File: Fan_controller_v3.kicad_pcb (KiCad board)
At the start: 4 copper layers, 50 x 25 mm, 52 parts, among them J1 Load2, J2 Dig_mod_iface, K1 HFD2_005-S-L2-D_Split, K2 HFD2_005-S-L2-D_Split, Q1 2N5551S, Q2 2N5551S, Q3 BSS138, Q4 BSS138, Q5 2N5551S, Q6 2N5551S, U1 ADuM1251ARZ, U2 PCA9536DP

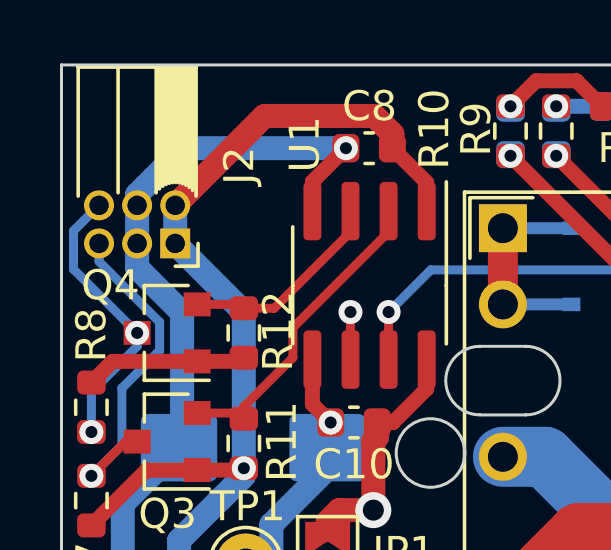
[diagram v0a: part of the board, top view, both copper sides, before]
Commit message: Сформирован перечень элементов, 3D-модель, исправлены ошибки, реализована панелизация платы.
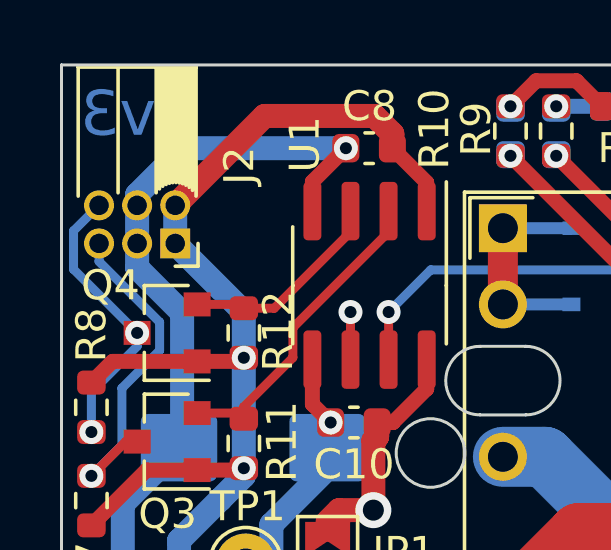
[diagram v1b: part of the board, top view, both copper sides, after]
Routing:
- net +5P: vias 1 -> 2
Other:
- board text added: "v3"

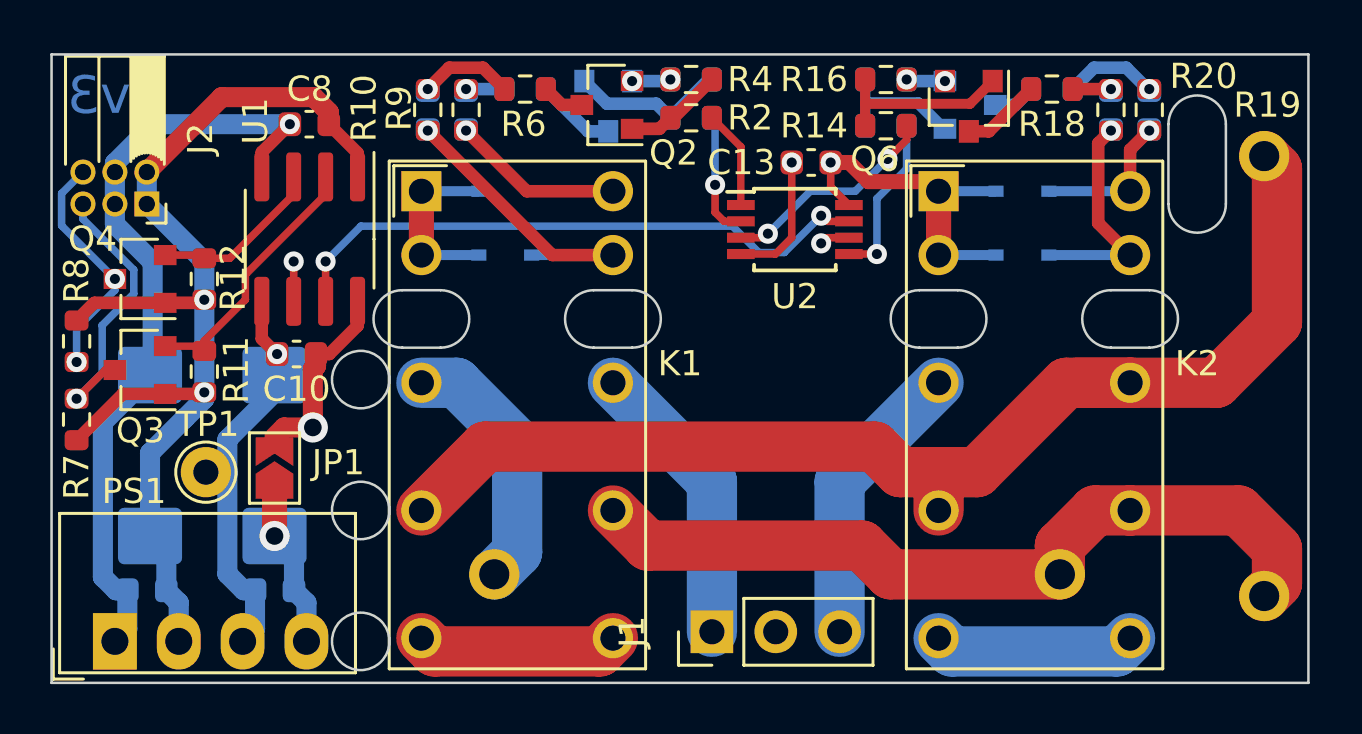
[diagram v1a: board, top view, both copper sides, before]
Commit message: Добавил отверстия в виде футпринтов и обновил гербера. Схему пока не менял.
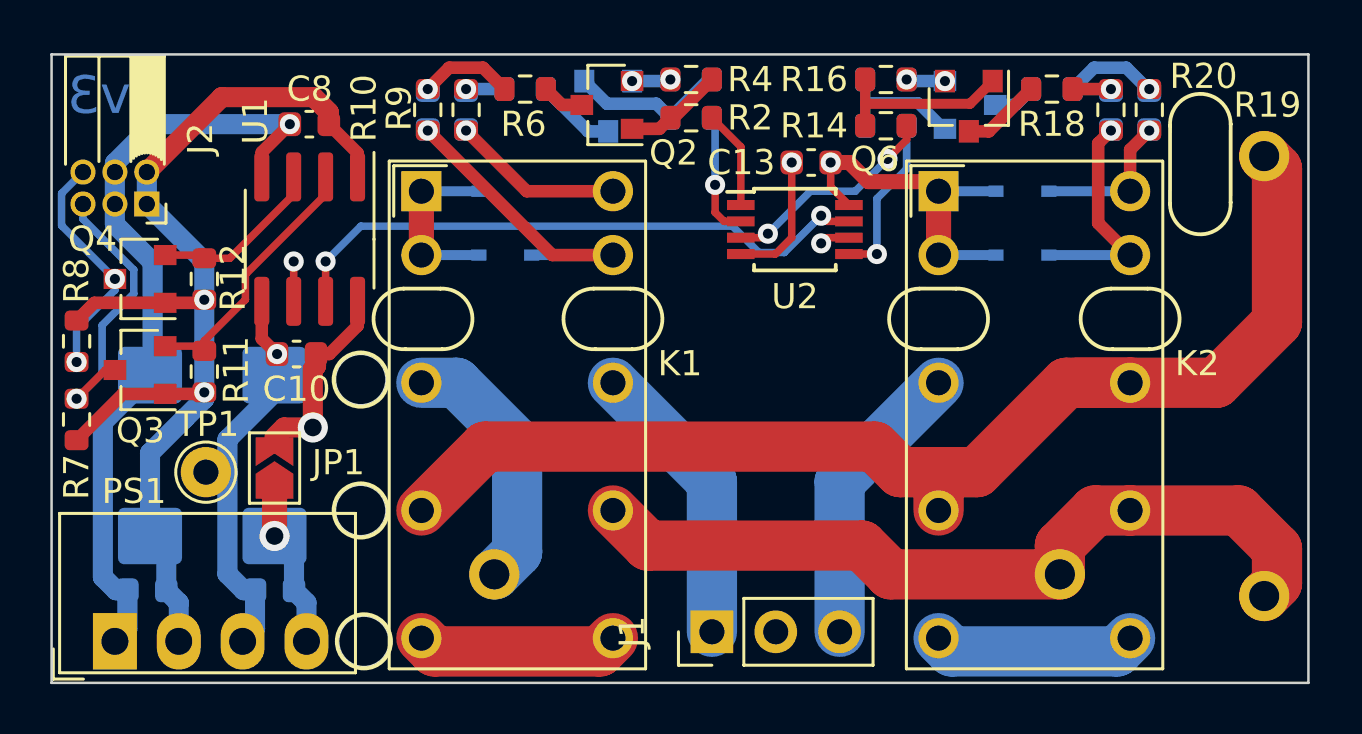
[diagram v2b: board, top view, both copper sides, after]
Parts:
- added REF**: MountingHole_2.29x5.46mm, Modules:MountingHole_2.29x5.46mm, F.Cu at (120.7, 79.4)
- added REF**: MountingHole_2.29x3.81mm, Modules:MountingHole_2.29x3.81mm, F.Cu at (117.9, 85.5)
- added REF**: MountingHole_2.29x3.81mm, Modules:MountingHole_2.29x3.81mm, F.Cu at (110.3, 85.5)
- added REF**: MountingHole_2.29x3.81mm, Modules:MountingHole_2.29x3.81mm, F.Cu at (97.3, 85.5)
- added REF**: MountingHole_2.29x3.81mm, Modules:MountingHole_2.29x3.81mm, F.Cu at (89.8, 85.5)
- added REF**: MountingHole_D2.0mm, Modules:MountingHole_D2.0mm, F.Cu at (87.3, 87.9)
- added REF**: MountingHole_D2.0mm, Modules:MountingHole_D2.0mm, F.Cu at (87.3, 93.1)
- added REF**: MountingHole_D2.0mm, Modules:MountingHole_D2.0mm, F.Cu at (87.4, 98.3)
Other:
- outline, holes or cut-outs redrawn

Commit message: Добавил изолирующие отверстия на схему. Подправил компоненты отверстий. Удалил контуры отверстий на обеих слоях платы.
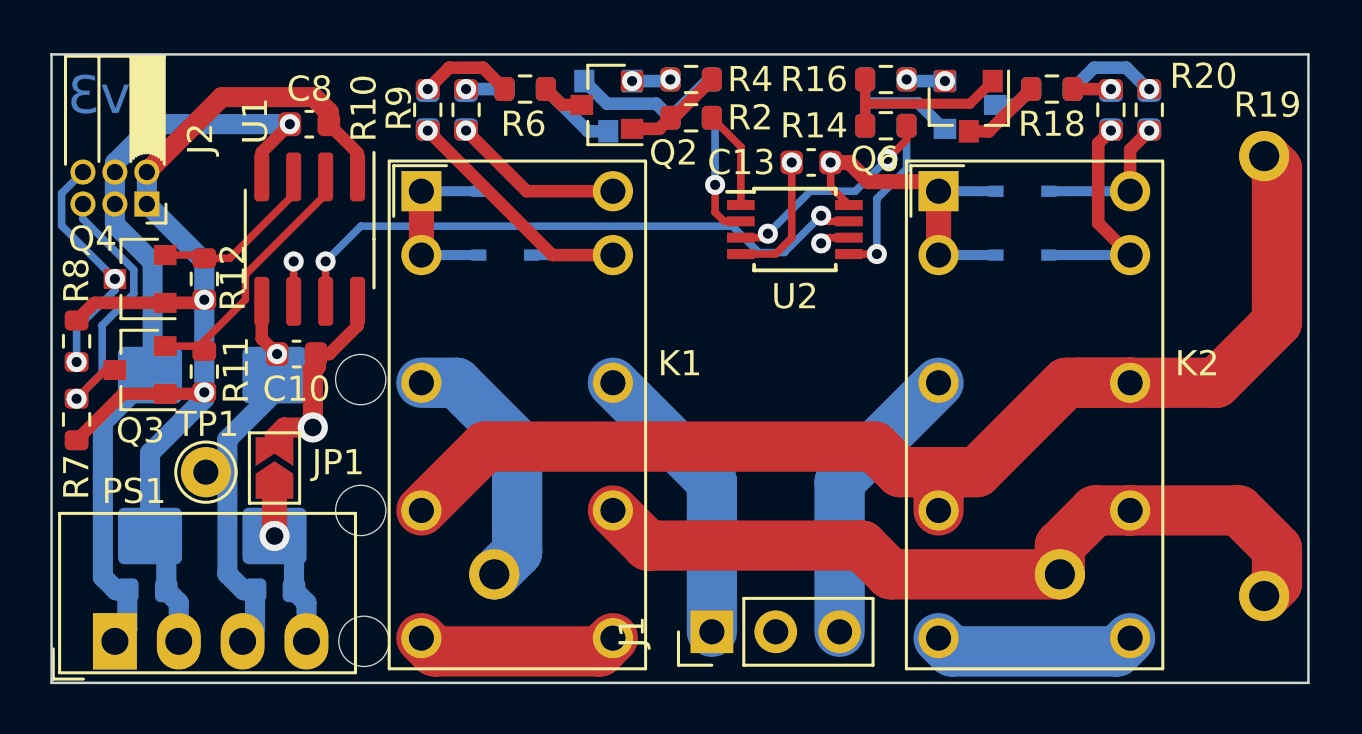
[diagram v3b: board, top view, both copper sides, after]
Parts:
- removed REF**: MountingHole_2.29x5.46mm, Modules:MountingHole_2.29x5.46mm
- removed REF** (x4): MountingHole_2.29x3.81mm, Modules:MountingHole_2.29x3.81mm
- removed REF** (x3): MountingHole_D2.0mm, Modules:MountingHole_D2.0mm
- added H1: MountingHole_D2.0mm, Modules:MountingHole_D2.0mm, F.Cu at (87.3, 87.9)
- added H2: MountingHole_D2.0mm, Modules:MountingHole_D2.0mm, F.Cu at (87.3, 93.1)
- added H3: MountingHole_D2.0mm, Modules:MountingHole_D2.0mm, F.Cu at (87.4, 98.3)
- added H4: MountingHole_2.29x3.81mm, Modules:MountingHole_2.29x3.81mm, F.Cu at (89.8, 85.5)
- added H5: MountingHole_2.29x3.81mm, Modules:MountingHole_2.29x3.81mm, F.Cu at (97.3, 85.5)
- added H6: MountingHole_2.29x3.81mm, Modules:MountingHole_2.29x3.81mm, F.Cu at (110.3, 85.5)
- added H7: MountingHole_2.29x3.81mm, Modules:MountingHole_2.29x3.81mm, F.Cu at (117.9, 85.5)
- added H8: MountingHole_2.29x5.46mm, Modules:MountingHole_2.29x5.46mm, F.Cu at (120.7, 79.4)
